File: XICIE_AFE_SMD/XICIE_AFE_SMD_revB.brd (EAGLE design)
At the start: 101 x 60.4 mm, 34 parts, among them IC1 LM324D, IC2 CY8C4245T, IC3 AAT1217, J1 22-27-2021-02, Q1 MOSFET-NCHANNELBSS123LT1G, Q2 MOSFET-NCHANNELBSS123LT1G

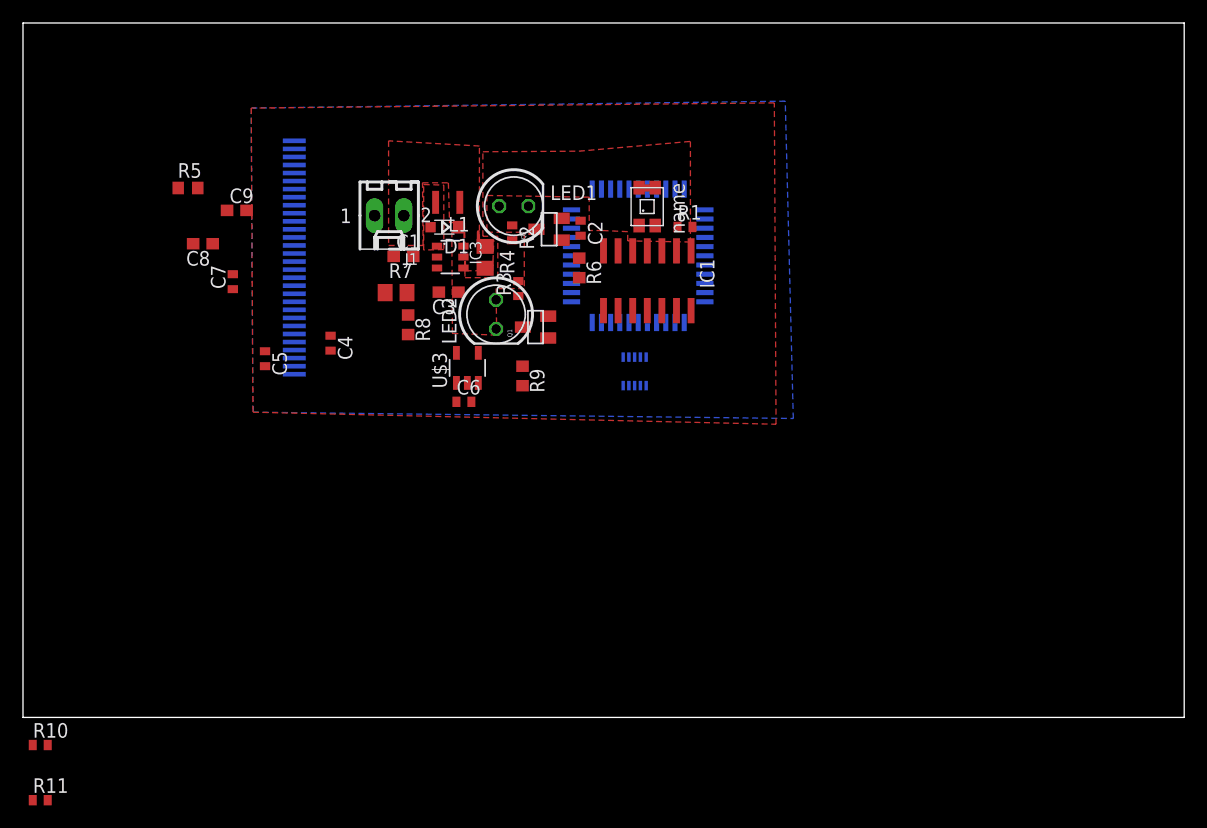
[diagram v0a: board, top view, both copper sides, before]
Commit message: Increased clearance for better manufacturing
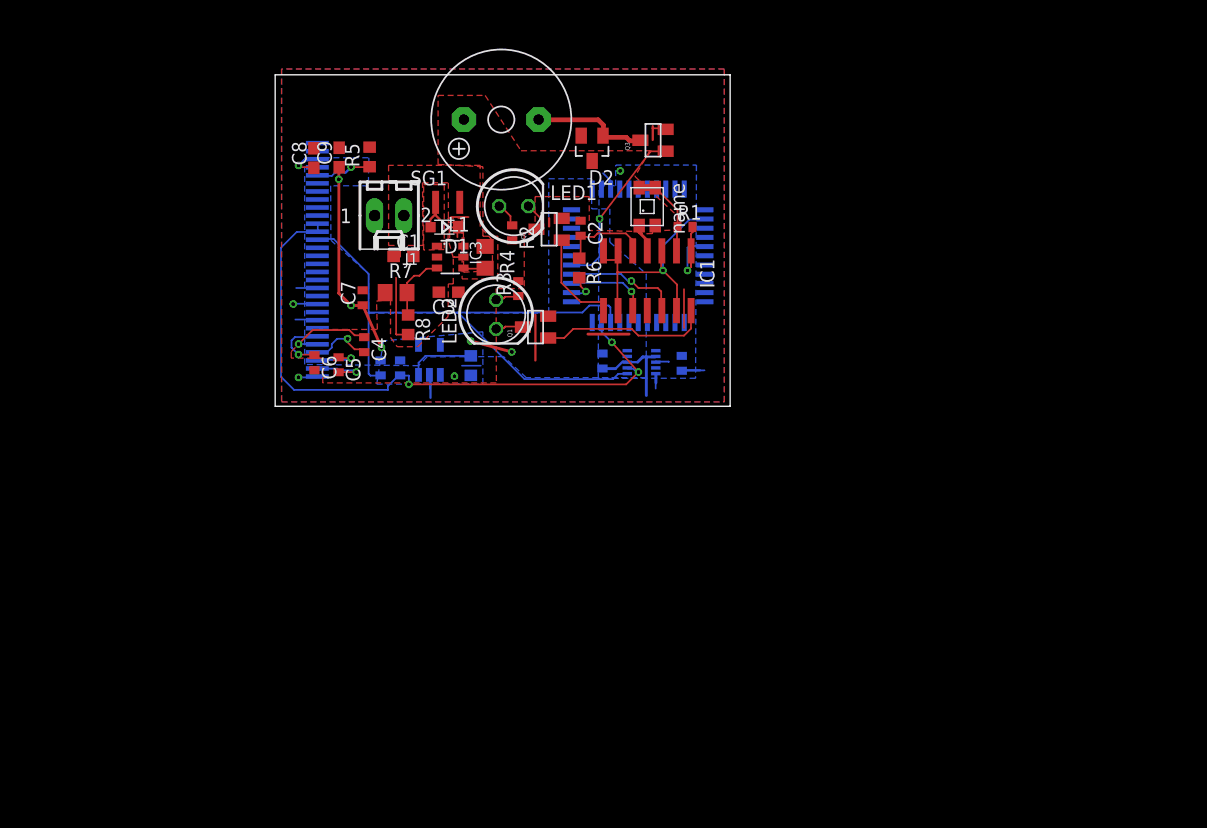
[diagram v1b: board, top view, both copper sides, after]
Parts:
- added C10, C11: 0.1 uF, rcl:C0402
- added D2: (no value), diode:SOT23
- added Q3: MOSFET-NCHANNELBSS123LT1G, SparkFun-DiscreteSemi:SOT23
- added SG1: F/QMX, buzzer:F/QMX
- moved R11 48.9 mm to (35.2, 50.2), flipped to the bottom, turned to 90 degrees
- moved R10 44.2 mm to (33.5, 50.2), flipped to the bottom, turned to 90 degrees
- moved R5 16.0 mm to (32.5, 68.5), turned to 90 degrees
- moved C6 13.4 mm to (27.8, 50.6), turned to 270 degrees
- moved C8 12.2 mm to (27.7, 68.5), turned to 90 degrees
- moved C7 11.4 mm to (31.9, 56.3)
- moved C9 10.0 mm to (29.9, 68.5), turned to 90 degrees
- moved C5 6.42 mm to (29.8, 50.5)
- moved R9 4.59 mm to (41.4, 50.4), flipped to the bottom, turned to 90 degrees
- moved U$3 3.37 mm to (37.8, 50.9), flipped to the bottom
- moved C4 2.93 mm to (32.1, 52.2)
- moved U$2 2.01 mm to (28.0, 59.6)
- moved U$4 1.00 mm to (56.2, 50.7), turned to 90 degrees
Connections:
- new net BUZZ: IC2.27, Q3.1
- new net N$13: D2.1, Q3.3, SG1.-
- net +3V3: now also C11.1, D2.3, SG1.+
- net GND: now also C10.2, C11.2, Q3.2
- net VCC: now also C10.1
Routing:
- net SDA: track 0.00 -> 55.9 mm, vias 0 -> 3
- net SCL: track 0.00 -> 55.5 mm
- net GND: track 0.00 -> 46.5 mm, vias 0 -> 2
- net VREF: track 0.00 -> 24.6 mm, vias 0 -> 1
- net VCC: track 0.00 -> 21.5 mm, vias 0 -> 5
- net +3V3: track 0.00 -> 14.8 mm, vias 0 -> 3
- net N$4: track 0.00 -> 14.8 mm
- net BUZZ: track 0.00 -> 14.7 mm, vias 0 -> 1
- net N$13: track 0.00 -> 10.6 mm
- net IR: track 0.00 -> 10.1 mm, vias 0 -> 1
- net SENSOROUT: track 0.00 -> 9.02 mm, vias 0 -> 1
- net N$3: track 0.00 -> 8.82 mm
- net C1N: track 0.00 -> 8.08 mm, vias 0 -> 1
- net N$9: track 0.00 -> 7.87 mm
- net N$1: track 0.00 -> 7.72 mm
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- added copper zone on layer 16, net +3V3
- added copper zone on layer 16, net VCC
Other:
- board size 101 x 60.4 mm -> 39.6 x 28.8 mm

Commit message: Added revision B of board
Included MMA interrupt and bypass capacitors for psoc.
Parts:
- added C12, C14, C17: 0.1 uF, rcl:C0402
- added C13, C15, C16: 1 uF, rcl:C0402
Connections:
- new net !MMA_INT: IC2.28
- new net N$10: C16.1, IC2.33
- net +3V3: no longer IC2.35
- net GND: now also C12.2, C13.2, C14.2, C15.2, C16.2, C17.2
- net VCC: now also C12.1, C13.1, C14.1, C15.1, C17.1, IC2.35; no longer IC2.33
